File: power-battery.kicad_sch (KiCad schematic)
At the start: 6 parts, among them J2 JSTPH, U3 MCP73831-2-OT

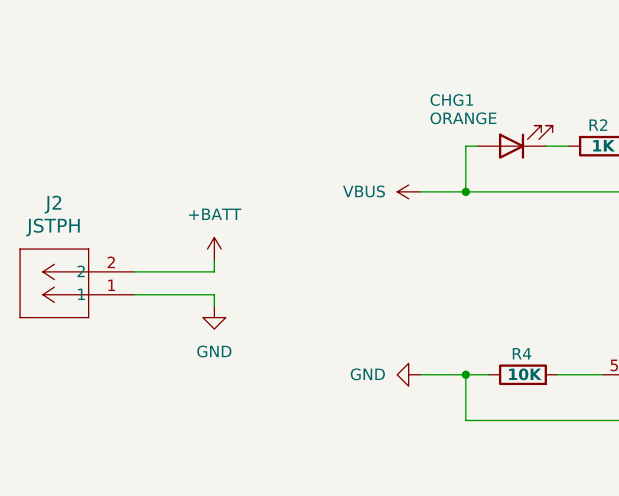
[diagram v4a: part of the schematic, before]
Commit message: Added mounting holes
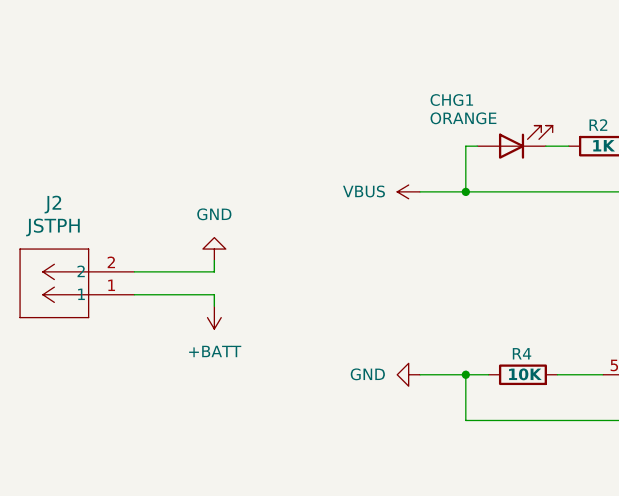
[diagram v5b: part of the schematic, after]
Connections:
- net +BATT: now also J2.1; no longer J2.2
- net GND: now also J2.2; no longer J2.1
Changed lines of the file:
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@@
-	)
-	(symbol
-		(lib_id "power:+BATT")
-		(at 111.76 96.52 0)
-		(unit 1)
-		(exclude_from_sim no)
-		(in_bom yes)
-		(on_board yes)
-		(dnp no)
-		(fields_autoplaced yes)
-		(property "Reference" "#PWR034"
-			(at 111.76 100.33 0)
-			(effects
-				(font
-					(size 1.27 1.27)
-				)
-				(hide yes)
-			)
-		)
-		(property "Value" "+BATT"
-			(at 111.76 91.44 0)
-			(effects
-				(font
-					(size 1.27 1.27)
-				)
-			)
-		)
-		(property "Footprint" ""
-			(at 111.76 96.52 0)
-			(effects
-				(font
-					(size 1.27 1.27)
-				)
-				(hide yes)
-			)
-		)
-		(property "Datasheet" ""
-			(at 111.76 96.52 0)
-			(effects
-				(font
-					(size 1.27 1.27)
-				)
-				(hide yes)
-			)
-		)
-		(property "Description" "Power symbol creates a global label with name \"+BATT\""
-			(at 111.76 96.52 0)
-			(effects
-				(font
-					(size 1.27 1.27)
-				)
-				(hide yes)
-			)
-		)
-		(pin "1"
-		)
-		(instances
-			(project "roamer"
-				(path "/1c59de6a-87fe-4223-8898-4b0383164a31/8b882434-0721-40fe-a26c-3dd045b3f675"
-					(reference "#PWR034")
-					(unit 1)
-				)
-			)
-		)
 	)
 	(symbol
@@
 	(symbol
 		(lib_id "power:GND")
-		(at 111.76 101.6 0)
+		(at 111.76 96.52 180)
 		(unit 1)
 		(exclude_from_sim no)
@@
 		(fields_autoplaced yes)
 		(property "Reference" "#PWR033"
-			(at 111.76 107.95 0)
+			(at 111.76 90.17 0)
 			(effects
 				(font
@@
 		)
 		(property "Value" "GND"
-			(at 111.76 106.68 0)
+			(at 111.76 91.44 0)
 			(effects
 				(font
@@
 		)
 		(property "Footprint" ""
-			(at 111.76 101.6 0)
+			(at 111.76 96.52 0)
 			(effects
 				(font
@@
 		)
 		(property "Datasheet" ""
-			(at 111.76 101.6 0)
+			(at 111.76 96.52 0)
 			(effects
 				(font
@@
 		)
 		(property "Description" "Power symbol creates a global label with name \"GND\" , ground"
-			(at 111.76 101.6 0)
+			(at 111.76 96.52 0)
 			(effects
 				(font
@@
 					(unit 1)
 				)
+			)
+		)
+	)
+	(symbol
+		(lib_id "power:+BATT")
+		(at 111.76 101.6 180)
+		(unit 1)
+		(exclude_from_sim no)
+		(in_bom yes)
+		(on_board yes)
+		(dnp no)
+		(fields_autoplaced yes)
+		(property "Reference" "#PWR034"
+			(at 111.76 97.79 0)
+			(effects
+				(font
+					(size 1.27 1.27)
+				)
+				(hide yes)
+			)
+		)
+		(property "Value" "+BATT"
+			(at 111.76 106.68 0)
+			(effects
+				(font
+					(size 1.27 1.27)
+				)
+			)
+		)
+		(property "Footprint" ""
+			(at 111.76 101.6 0)
+			(effects
+				(font
+					(size 1.27 1.27)
+				)
+				(hide yes)
+			)
+		)
+		(property "Datasheet" ""
+			(at 111.76 101.6 0)
+			(effects
+				(font
+					(size 1.27 1.27)
+				)
+				(hide yes)
+			)
+		)
+		(property "Description" "Power symbol creates a global label with name \"+BATT\""
+			(at 111.76 101.6 0)
+			(effects
+				(font
+					(size 1.27 1.27)
+				)
+				(hide yes)
+			)
+		)
+		(pin "1"
+		)
+		(instances
+			(project "roamer"
+				(path "/1c59de6a-87fe-4223-8898-4b0383164a31/8b882434-0721-40fe-a26c-3dd045b3f675"
+					(reference "#PWR034")
+					(unit 1)
+				)
